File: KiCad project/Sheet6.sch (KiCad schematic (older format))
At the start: 1 part

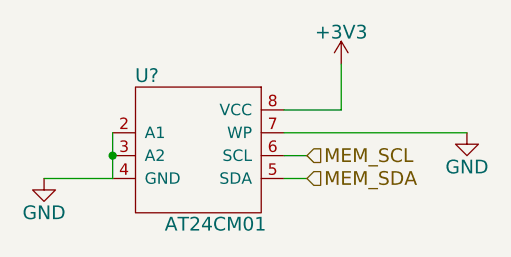
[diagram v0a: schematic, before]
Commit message: IC packages, bugfixes
drawings for IC packages, associations, schematic fixes
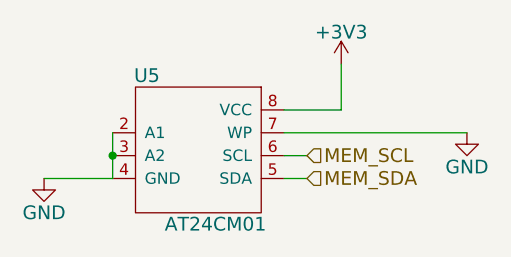
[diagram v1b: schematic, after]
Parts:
- U5: renamed from U?; footprint (none) -> Housings_SOIC:SOIC-8_3.9x4.9mm_Pitch1.27mm
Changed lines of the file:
@@
 $Descr A4 11693 8268
 encoding utf-8
-Sheet 7 7
+Sheet 7 10
 Title "AT24C1024"
 Date "16 March 2015"
@@
 $EndDescr
 $Comp
-L GND #PWR42
+L GND #PWR030
 U 1 1 55079275
 P 4700 1500
-F 0 "#PWR42" H 4700 1250 60  0001 C CNN
+F 0 "#PWR030" H 4700 1250 60  0001 C CNN
 F 1 "GND" H 4700 1350 60  0000 C CNN
 F 2 "" H 4700 1500 60  0000 C CNN
@@
 $EndComp
 $Comp
-L +3V3 #PWR41
+L +3V3 #PWR031
 U 1 1 55079289
 P 4150 1200
-F 0 "#PWR41" H 4150 1050 60  0001 C CNN
+F 0 "#PWR031" H 4150 1050 60  0001 C CNN
 F 1 "+3V3" H 4150 1340 60  0000 C CNN
 F 2 "" H 4150 1200 60  0000 C CNN
@@
 	3900 1700 4000 1700
 $Comp
-L AT24CM01 U?
+L AT24CM01 U5
 U 1 1 55079484
 P 3250 1300
-F 0 "U?" H 3300 1350 60  0000 C CNN
+F 0 "U5" H 3300 1350 60  0000 C CNN
 F 1 "AT24CM01" H 3600 700 60  0000 C CNN
-F 2 "" H 3250 1300 60  0000 C CNN
+F 2 "Housings_SOIC:SOIC-8_3.9x4.9mm_Pitch1.27mm" H 3250 1300 60  0001 C CNN
 F 3 "" H 3250 1300 60  0000 C CNN
 	1    3250 1300
@@
 $EndComp
 $Comp
-L GND #PWR?
+L GND #PWR032
 U 1 1 550794AD
 P 2850 1700
-F 0 "#PWR?" H 2850 1450 60  0001 C CNN
+F 0 "#PWR032" H 2850 1450 60  0001 C CNN
 F 1 "GND" H 2850 1550 60  0000 C CNN
 F 2 "" H 2850 1700 60  0000 C CNN

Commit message: New packages, PCB
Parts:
- renumbered U5 to U6
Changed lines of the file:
@@
 $EndDescr
 $Comp
-L GND #PWR030
+L GND #PWR029
 U 1 1 55079275
 P 4700 1500
-F 0 "#PWR030" H 4700 1250 60  0001 C CNN
+F 0 "#PWR029" H 4700 1250 60  0001 C CNN
 F 1 "GND" H 4700 1350 60  0000 C CNN
 F 2 "" H 4700 1500 60  0000 C CNN
@@
 $EndComp
 $Comp
-L +3V3 #PWR031
+L +3V3 #PWR030
 U 1 1 55079289
 P 4150 1200
-F 0 "#PWR031" H 4150 1050 60  0001 C CNN
+F 0 "#PWR030" H 4150 1050 60  0001 C CNN
 F 1 "+3V3" H 4150 1340 60  0000 C CNN
 F 2 "" H 4150 1200 60  0000 C CNN
@@
 	3900 1700 4000 1700
 $Comp
-L AT24CM01 U5
+L AT24CM01 U6
 U 1 1 55079484
 P 3250 1300
-F 0 "U5" H 3300 1350 60  0000 C CNN
+F 0 "U6" H 3300 1350 60  0000 C CNN
 F 1 "AT24CM01" H 3600 700 60  0000 C CNN
 F 2 "Housings_SOIC:SOIC-8_3.9x4.9mm_Pitch1.27mm" H 3250 1300 60  0001 C CNN
@@
 $EndComp
 $Comp
-L GND #PWR032
+L GND #PWR031
 U 1 1 550794AD
 P 2850 1700
-F 0 "#PWR032" H 2850 1450 60  0001 C CNN
+F 0 "#PWR031" H 2850 1450 60  0001 C CNN
 F 1 "GND" H 2850 1550 60  0000 C CNN
 F 2 "" H 2850 1700 60  0000 C CNN

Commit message: Refactoring
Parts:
- U6: value AT24CM01 -> AT24C256
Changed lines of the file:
@@
 LIBS:memory
 LIBS:xilinx
-LIBS:special
 LIBS:microcontrollers
 LIBS:dsp
@@
 P 3250 1300
 F 0 "U6" H 3300 1350 60  0000 C CNN
-F 1 "AT24CM01" H 3600 700 60  0000 C CNN
+F 1 "AT24C256" H 3600 700 60  0000 C CNN
 F 2 "Housings_SOIC:SOIC-8_3.9x4.9mm_Pitch1.27mm" H 3250 1300 60  0001 C CNN
 F 3 "" H 3250 1300 60  0000 C CNN
